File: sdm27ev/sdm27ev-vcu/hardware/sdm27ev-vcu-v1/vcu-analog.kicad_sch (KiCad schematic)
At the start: 0 parts

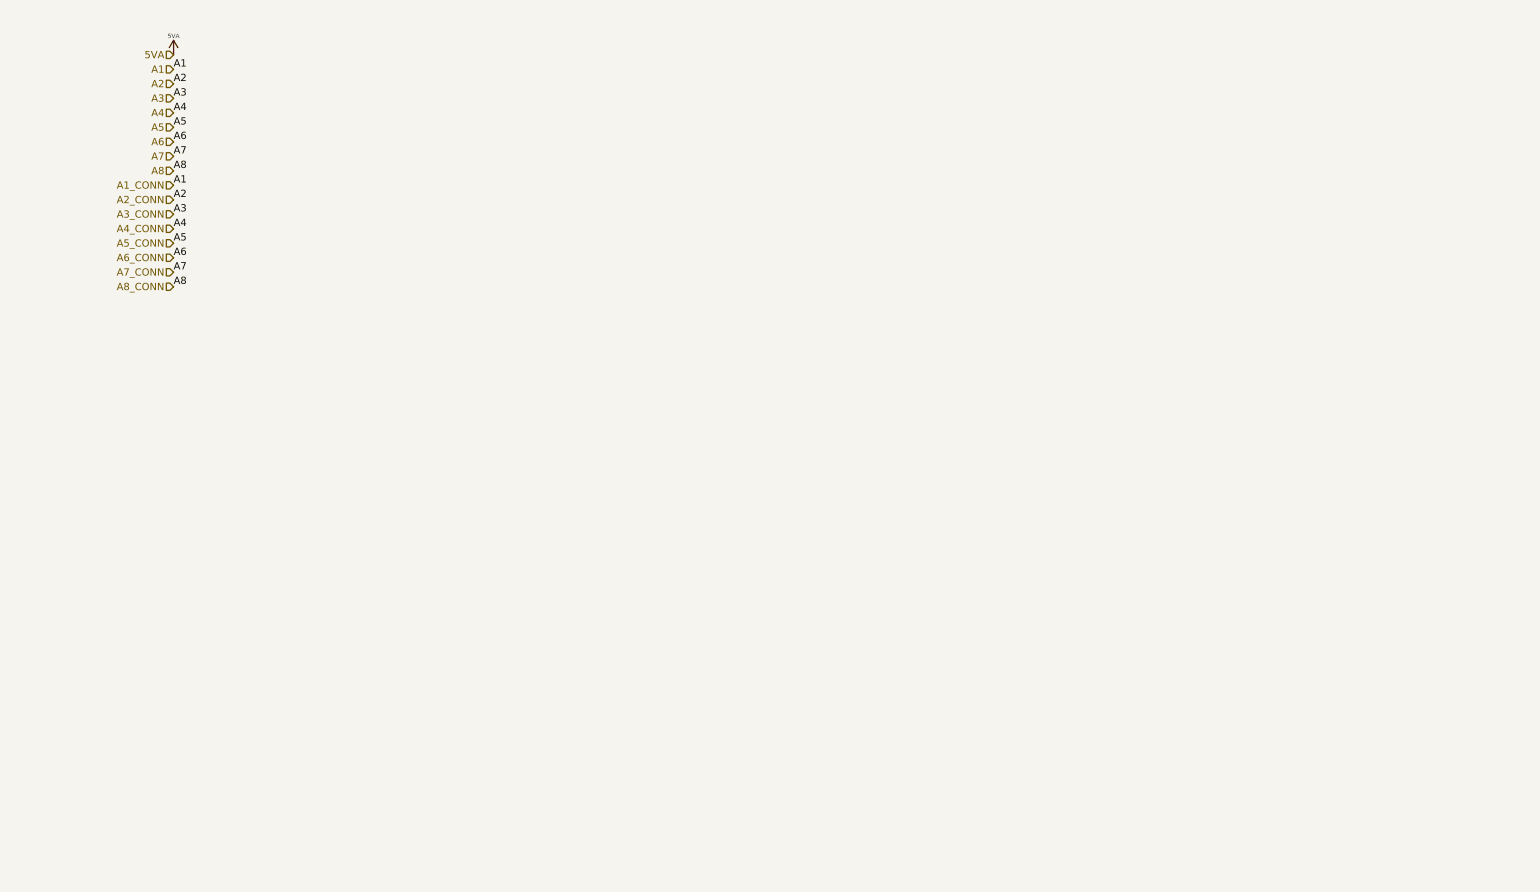
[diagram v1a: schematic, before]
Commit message: EV27 VCU, analog front end. still needs analog power protection
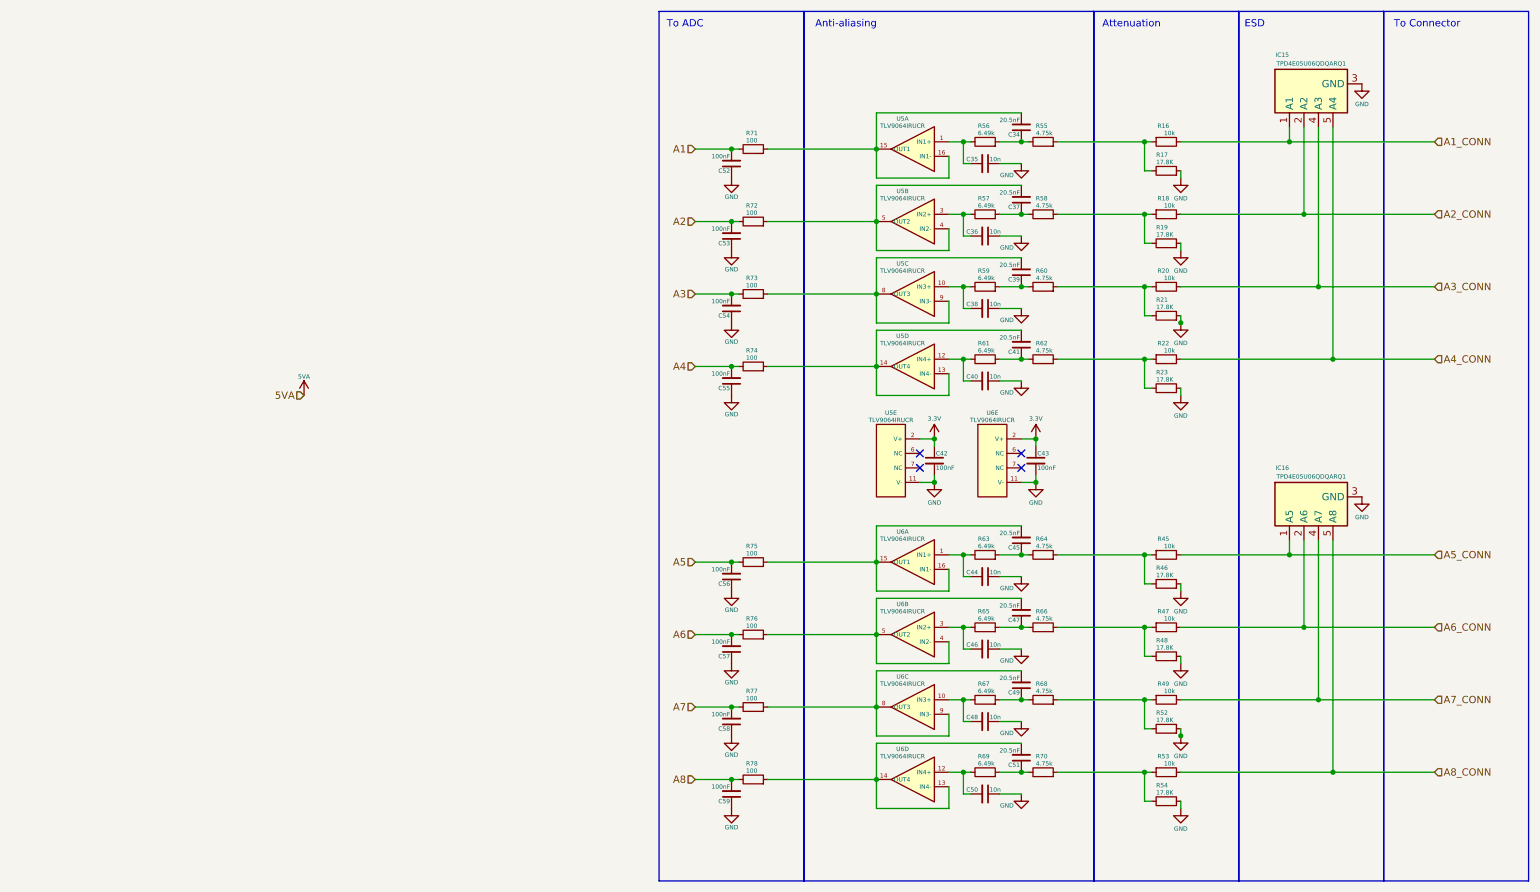
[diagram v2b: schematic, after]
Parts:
- added C34, C37, C39, C41, C45, C47, C49, C51: 20.5nF, Capacitor_SMD:C_0603_1608Metric, symbol Device:C_Small
- added C35, C36, C38, C40, C44, C46, C48, C50: 10n, Capacitor_SMD:C_0603_1608Metric, symbol Device:C_Small
- added C42, C43, C52, C53, C54, C55, C56, C57, C58, C59: 100nF, Capacitor_SMD:C_0603_1608Metric, symbol Device:C_Small
- added IC15, IC16: TPD4E05U06QDQARQ1, DQA(R-PUSON-N10), symbol SDM_EV:TPD4E05U06QDQARQ1
- added R16, R18, R20, R22, R45, R47, R49, R53: 10k, Resistor_SMD:R_0603_1608Metric, symbol Device:R_Small
- added R17, R19, R21, R23, R46, R48, R52, R54: 17.8K, Resistor_SMD:R_0603_1608Metric, symbol Device:R_Small
- added R55, R58, R60, R62, R64, R66, R68, R70: 4.75k, Resistor_SMD:R_0603_1608Metric, symbol Device:R_Small
- added R56, R57, R59, R61, R63, R65, R67, R69: 6.49k, Resistor_SMD:R_0603_1608Metric, symbol Device:R_Small
- added R71, R72, R73, R74, R75, R76, R77, R78: 100, Resistor_SMD:R_0603_1608Metric, symbol Device:R_Small
- added U5, U6: TLV9064IRUCR, symbol SDM_EV:TLV9064IRUCR
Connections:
- net A1: now also C52.2, R71.2
- net A2: now also C53.2, R72.2
- net A3: now also C54.2, R73.2
- net A4: now also C55.2, R74.2
- net A5: now also C56.2, R75.2
- net A6: now also C57.2, R76.2
- net A7: now also C58.2, R77.2
- net A8: now also C59.2, R78.2
- new net: R53.1, R54.2, R70.1
- new net: C41.1, R61.1, R62.2
- new net: C41.2, R74.1, U5.13 (IN4-), U5.14 (OUT4)
- new net: C39.1, R59.1, R60.2
- new net: C39.2, R73.1, U5.8 (OUT3), U5.9 (IN3-)
- new net: C37.1, R57.1, R58.2
- new net: C36.2, R57.2, U5.3 (IN2+)
- new net: R20.1, R21.2, R60.1
- new net: C34.1, R55.2, R56.1
- new net: C34.2, R71.1, U5.15 (OUT1), U5.16 (IN1-)
- new net: C40.2, R61.2, U5.12 (IN4+)
- new net: C35.2, R56.2, U5.1 (IN1+)
- new net: R18.1, R19.2, R58.1
- new net: C38.2, R59.2, U5.10 (IN3+)
- new net: C51.2, R78.1, U6.13 (IN4-), U6.14 (OUT4)
- new net: C44.2, R63.2, U6.1 (IN1+)
- new net: C51.1, R69.1, R70.2
- new net: C50.2, R69.2, U6.12 (IN4+)
- new net: C45.2, R75.1, U6.15 (OUT1), U6.16 (IN1-)
- new net: C46.2, R65.2, U6.3 (IN2+)
- new net: C48.2, R67.2, U6.10 (IN3+)
- new net: C49.2, R77.1, U6.8 (OUT3), U6.9 (IN3-)
- new net: R22.1, R23.2, R62.1
- new net: IC15.10 (NC_3), IC15.6 (NC_4), IC15.7 (NC_1), IC15.9 (NC_2)
- new net: R49.1, R52.2, R68.1
- new net: C49.1, R67.1, R68.2
- new net: R16.1, R17.2, R55.1
- new net: R45.1, R46.2, R64.1
- new net: C47.2, R76.1, U6.4 (IN2-), U6.5 (OUT2)
- new net: C47.1, R65.1, R66.2
- new net: C45.1, R63.1, R64.2
- new net: C37.2, R72.1, U5.4 (IN2-), U5.5 (OUT2)
- new net: R47.1, R48.2, R66.1
- new net: IC16.10 (NC_3), IC16.6 (NC_4), IC16.7 (NC_1), IC16.9 (NC_2)
- new net 3.3V: C42.1, C43.1, U5.2 (V+), U6.2 (V+)
- new net A1_CONN: IC15.1 (A1), R16.2
- new net A2_CONN: IC15.2 (A2), R18.2
- new net A3_CONN: IC15.4 (A3), R20.2
- new net A4_CONN: IC15.5 (A4), R22.2
- new net A5_CONN: IC16.1 (A5), R45.2
- new net A6_CONN: IC16.2 (A6), R47.2
- new net A7_CONN: IC16.4 (A7), R49.2
- new net A8_CONN: IC16.5 (A8), R53.2
- new net GND: C35.1, C36.1, C38.1, C40.1, C42.2, C43.2, C44.1, C46.1, C48.1, C50.1, C52.1, C53.1, C54.1, C55.1, C56.1, C57.1, C58.1, C59.1, IC15.3 (GND), IC15.8 (GND_2), IC16.3 (GND), IC16.8 (GND_2), R17.1, R19.1, R21.1, R23.1, R46.1, R48.1, R52.1, R54.1, U5.11 (V-), U6.11 (V-)
- no-connect marks 0 -> 4
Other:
- note added: "Anti-aliasing"
- note added: "Attenuation"
- note added: "ESD"
- note added: "To ADC"
- note added: "To Connector"

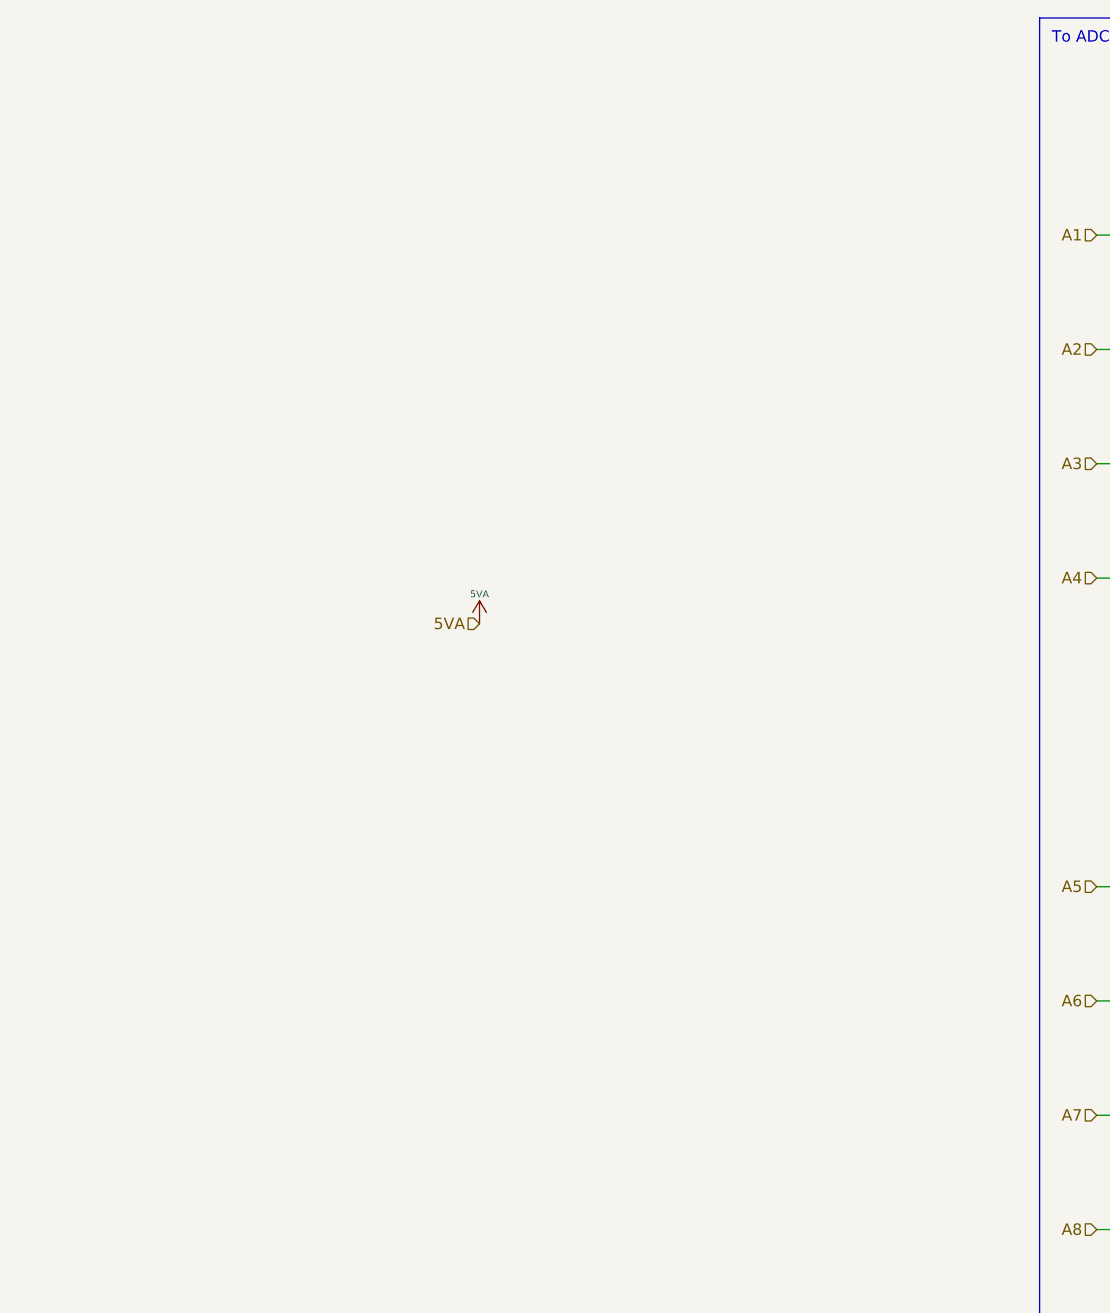
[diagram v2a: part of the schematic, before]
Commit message: Added analog power switch
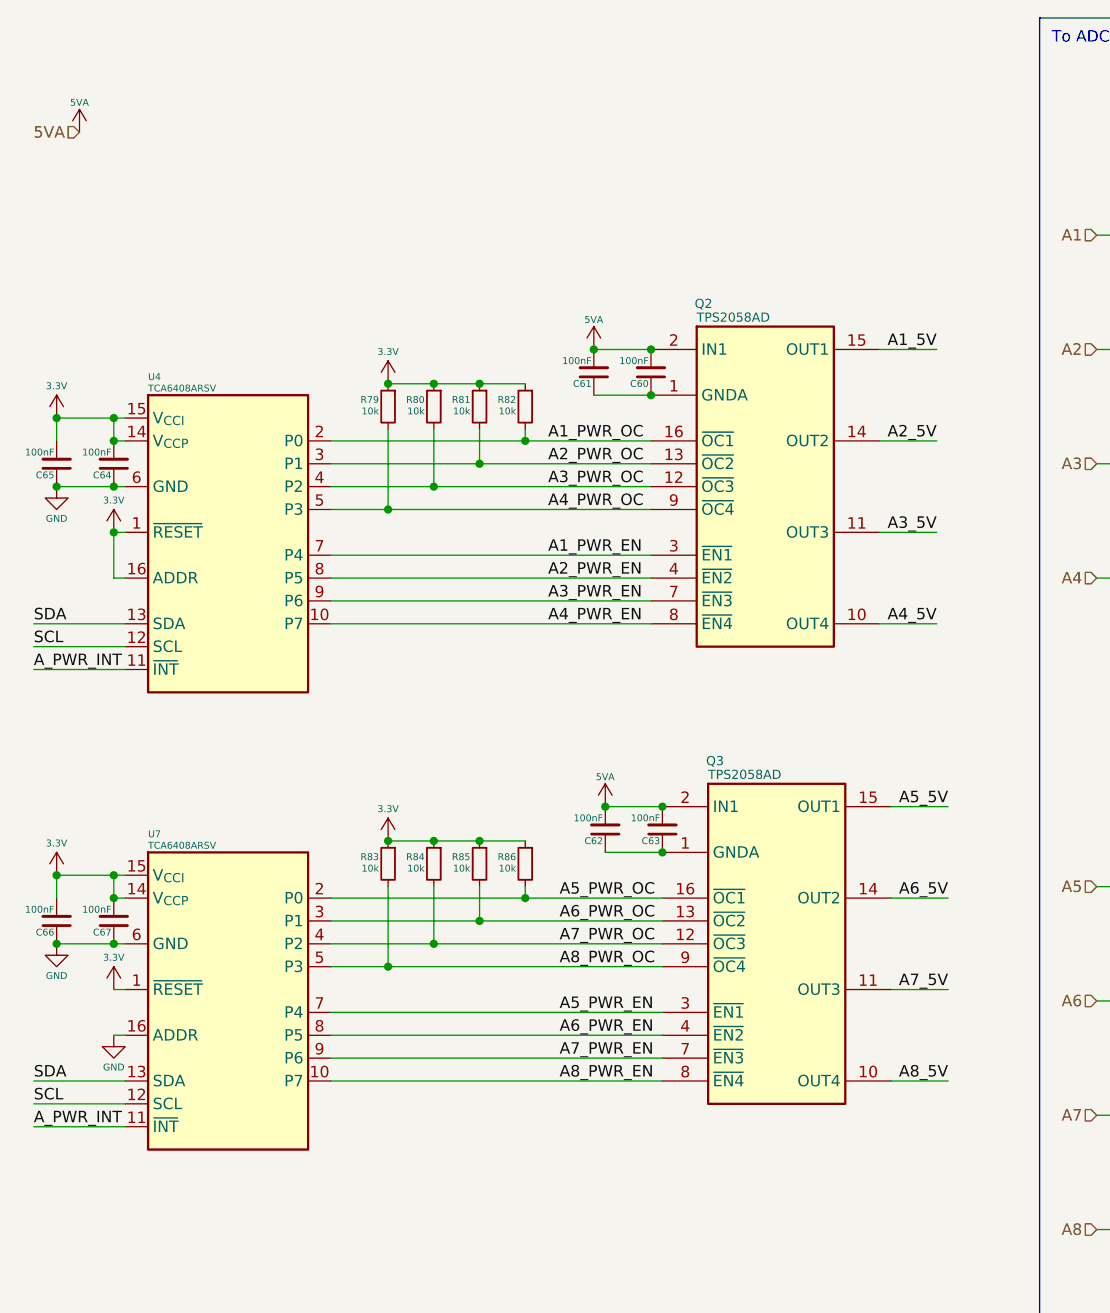
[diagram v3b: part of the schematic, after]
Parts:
- added C60, C61, C62, C63, C64, C65, C66, C67: 100nF, Capacitor_SMD:C_0603_1608Metric, symbol Device:C_Small
- added Q2, Q3: TPS2058AD, SOIC127P600X175-16N, symbol SDM_EV:TPS2058AD
- added R79, R80, R81, R82, R83, R84, R85, R86: 10k, Resistor_SMD:R_0603_1608Metric, symbol Device:R_Small
- added U4, U7: TCA6408ARSV, Package_DFN_QFN:UQFN-16_1.8x2.6mm_P0.4mm, symbol Interface_Expansion:TCA6408ARSV
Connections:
- net 3.3V: now also C64.2, C65.2, C66.2, C67.2, R79.1, R80.1, R81.1, R82.1, R83.1, R84.1, R85.1, R86.1, U4.1 (~{RESET}), U4.14 (V_{CCP}), U4.15 (V_{CCI}), U4.16 (ADDR), U7.1 (~{RESET}), U7.14 (V_{CCP}), U7.15 (V_{CCI})
- net 5VA: now also C60.2, C61.2, C62.2, C63.2, Q2.2 (IN1), Q2.6 (IN2), Q3.2 (IN1), Q3.6 (IN2)
- net GND: now also C64.1, C65.1, C66.1, C67.1, U4.6 (GND), U7.16 (ADDR), U7.6 (GND)
- new net: C60.1, C61.1, Q2.1 (GNDA), Q2.5 (GNDB)
- new net: C62.1, C63.1, Q3.1 (GNDA), Q3.5 (GNDB)
- new net A1_5V: Q2.15 (OUT1)
- new net A1_PWR_EN: Q2.3 (~{EN1}), U4.7 (P4)
- new net A1_PWR_OC: Q2.16 (~{OC1}), R82.2, U4.2 (P0)
- new net A2_5V: Q2.14 (OUT2)
- new net A2_PWR_EN: Q2.4 (~{EN2}), U4.8 (P5)
- new net A2_PWR_OC: Q2.13 (~{OC2}), R81.2, U4.3 (P1)
- new net A3_5V: Q2.11 (OUT3)
- new net A3_PWR_EN: Q2.7 (~{EN3}), U4.9 (P6)
- new net A3_PWR_OC: Q2.12 (~{OC3}), R80.2, U4.4 (P2)
- new net A4_5V: Q2.10 (OUT4)
- new net A4_PWR_EN: Q2.8 (~{EN4}), U4.10 (P7)
- new net A4_PWR_OC: Q2.9 (~{OC4}), R79.2, U4.5 (P3)
- new net A5_5V: Q3.15 (OUT1)
- new net A5_PWR_EN: Q3.3 (~{EN1}), U7.7 (P4)
- new net A5_PWR_OC: Q3.16 (~{OC1}), R86.2, U7.2 (P0)
- new net A6_5V: Q3.14 (OUT2)
- new net A6_PWR_EN: Q3.4 (~{EN2}), U7.8 (P5)
- new net A6_PWR_OC: Q3.13 (~{OC2}), R85.2, U7.3 (P1)
- new net A7_5V: Q3.11 (OUT3)
- new net A7_PWR_EN: Q3.7 (~{EN3}), U7.9 (P6)
- new net A7_PWR_OC: Q3.12 (~{OC3}), R84.2, U7.4 (P2)
- new net A8_5V: Q3.10 (OUT4)
- new net A8_PWR_EN: Q3.8 (~{EN4}), U7.10 (P7)
- new net A8_PWR_OC: Q3.9 (~{OC4}), R83.2, U7.5 (P3)
- new net A_PWR_INT: U4.11 (~{INT}), U7.11 (~{INT})
- new net SCL: U4.12 (SCL), U7.12 (SCL)
- new net SDA: U4.13 (SDA), U7.13 (SDA)
